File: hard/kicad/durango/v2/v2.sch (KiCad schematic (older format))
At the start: 50 parts, among them J1 NANOLINK, J10 STEP, J2 AUDIO IN, J3 IOx, Q1 BC548, Q2 BC548, Q3 BC548, Q307 BC548, U1 65C02, U10 74HC139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

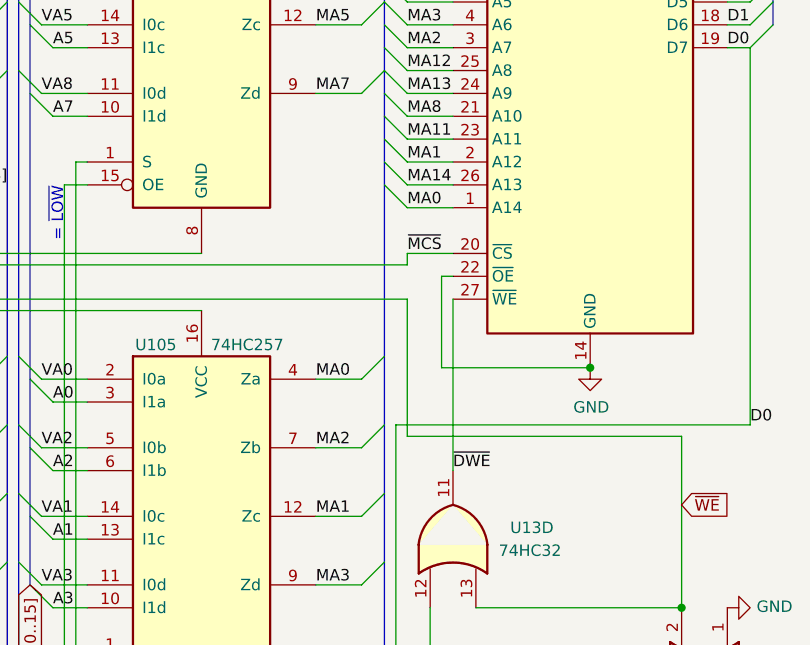
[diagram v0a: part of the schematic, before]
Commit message: add narrow SRAM footprint
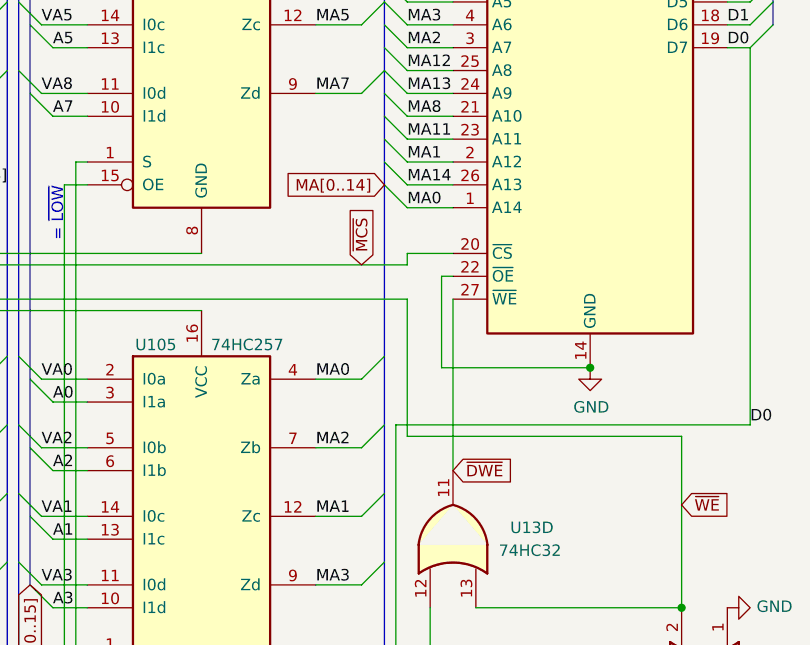
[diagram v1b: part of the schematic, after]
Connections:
- net IEN renamed MA[0..14]
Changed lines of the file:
@@
 Wire Wire Line
 	9400 2650 9200 2650
-Text Label 9200 2650 0    50   ~ 0
-~MCS
 Entry Wire Line
 	7500 4000 7600 4100
@@
 Wire Wire Line
 	9400 3600 9400 2850
-Text Label 9400 3600 0    50   ~ 0
-~DWE
 $Comp
 L power:GND #PWR0148
@@
 Wire Bus Line
 	4250 700  4250 6450
+Text GLabel 9100 2350 0    50   Input ~ 0
+MA[0..14]
+Text GLabel 9000 2700 1    50   Input ~ 0
+~MCS
+Text GLabel 9400 3600 2    50   Input ~ 0
+~DWE
 $EndSCHEMATC
